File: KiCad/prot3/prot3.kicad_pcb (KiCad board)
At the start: 2 copper layers, 140 x 140 mm, 198 parts, among them J1 Conn_01x02_Socket, J2 LED_SW, J3 Conn_01x04_Socket, Q1 Q_Photo_NPN, Q10 Q_Photo_NPN, Q11 Q_Photo_NPN, Q12 Q_Photo_NPN, Q13 Q_Photo_NPN, Q14 Q_Photo_NPN, Q15 Q_Photo_NPN, Q16 Q_Photo_NPN, Q17 Q_Photo_NPN, Q18 Q_Photo_NPN, Q19 Q_Photo_NPN, Q2 Q_Photo_NPN, Q20 Q_Photo_NPN, Q21 Q_Photo_NPN, Q22 Q_Photo_NPN, Q23 Q_Photo_NPN, Q24 Q_Photo_NPN, Q25 Q_Photo_NPN, Q26 Q_Photo_NPN, Q27 Q_Photo_NPN, Q28 Q_Photo_NPN, Q29 Q_Photo_NPN, Q3 Q_Photo_NPN, Q30 Q_Photo_NPN, Q31 Q_Photo_NPN, Q32 Q_Photo_NPN, Q4 Q_Photo_NPN, Q5 Q_Photo_NPN, Q6 Q_Photo_NPN, Q7 Q_Photo_NPN, Q8 Q_Photo_NPN, Q9 Q_Photo_NPN, U1 LM339, U2 LM339, U3 LM339, U4 LM339, U5 LM339, U6 LM339, U7 LM339, U8 LM339

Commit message: コンパレーター割当て途中
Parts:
- moved C14 133.4 mm to (526.1, 463.9)
- moved C15 133.4 mm to (526.1, 466.5)
- moved R1 133.4 mm to (526.1, 469.0)
- moved B1 120.3 mm to (525.6, 473.4)
- moved C8 107.1 mm to (532.6, 550.0), turned to -157.5 degrees
- moved C11 104.3 mm to (544.6, 480.9), turned to 90 degrees
- moved U8 98.6 mm to (526.3, 552.0), turned to 22.5 degrees
- moved Rc29 98.6 mm to (519.6, 553.0), turned to 22.5 degrees
- moved Rc31 93.6 mm to (531.6, 547.3), turned to -157.5 degrees
- moved Rc30 93.3 mm to (518.5, 550.3), turned to 22.5 degrees
- moved RP2040_Zero1 92.7 mm to (542.0, 479.0), turned to 90 degrees
- moved Rc32 88.6 mm to (530.5, 544.6), turned to -157.5 degrees
- moved C7 80.2 mm to (479.0, 554.4), turned to 157.5 degrees
- moved C9 77.0 mm to (532.8, 492.9)
- moved Rc25 75.3 mm to (467.2, 548.0), turned to -22.5 degrees
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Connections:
- C1 pad 2: LED_5V -> GND
- C10 pad 2: LED_5V -> GND
- C11 pad 2: LED_5V -> GND
- C12 pad 2: LED_5V -> GND
- C13 pad 2: LED_5V -> GND
- C15 pad 2: LED_5V -> GND
- C2 pad 2: LED_5V -> GND
- C3 pad 2: LED_5V -> GND
- C4 pad 2: LED_5V -> GND
- C5 pad 2: LED_5V -> GND
- C6 pad 2: LED_5V -> GND
- C7 pad 2: LED_5V -> GND
- C8 pad 2: LED_5V -> GND
- C9 pad 2: LED_5V -> GND
- J1 pad 2: LED_5V -> GND
- J3 pad 4: LED_5V -> GND
- Q1 pad 2: Net-(Q1-E) -> 1D
- Q10 pad 2: Net-(Q10-E) -> 3C
- Q11 pad 2: Net-(Q11-E) -> 4A
- Q12 pad 2: Net-(Q12-E) -> 4B
- Q13 pad 2: Net-(Q13-E) -> 4D
- Q14 pad 2: Net-(Q14-E) -> 4C
- Q15 pad 2: Net-(Q15-E) -> 5A
- Q16 pad 2: Net-(Q16-E) -> 5B
- Q17 pad 2: Net-(Q17-E) -> 5D
- Q18 pad 2: Net-(Q18-E) -> 6A
- Q19 pad 2: Net-(Q19-E) -> 6B
- Q2 pad 2: Net-(Q2-E) -> 1C
- Q20 pad 2: Net-(Q20-E) -> 6D
- Q21 pad 2: Net-(Q21-E) -> 7A
- Q22 pad 2: Net-(Q22-E) -> 7B
- Q23 pad 2: Net-(Q23-E) -> 7D
- Q24 pad 2: Net-(Q24-E) -> 7C
- Q25 pad 2: Net-(Q25-E) -> 8A
- Q26 pad 2: Net-(Q26-E) -> 8B
- Q27 pad 2: Net-(Q27-E) -> 8B
- Q28 pad 2: Net-(Q28-E) -> 8A
- Q29 pad 2: Net-(Q29-E) -> 8D
- Q3 pad 2: Net-(Q3-E) -> 2B
- Q30 pad 2: Net-(Q30-E) -> 8C
- Q31 pad 2: Net-(Q31-E) -> 1A
- Q32 pad 2: Net-(Q32-E) -> 1B
- Q4 pad 2: Net-(Q4-E) -> 2A
- Q5 pad 2: Net-(Q5-E) -> 2D
- Q6 pad 2: Net-(Q6-E) -> 2C
- Q7 pad 2: Net-(Q7-E) -> 3A
- Q8 pad 2: Net-(Q8-E) -> 3B
- Q9 pad 2: Net-(Q9-E) -> 3D
- RP2040_Zero1 pad 22: LED_5V -> GND
- RP2040_Zero2 pad 22: LED_5V -> GND
- RV1 pad 3: LED_5V -> GND
- Rl1 pad 2: LED_5V -> GND
- Rl10 pad 2: LED_5V -> GND
- Rl11 pad 2: LED_5V -> GND
- Rl12 pad 2: LED_5V -> GND
- Rl13 pad 2: LED_5V -> GND
- Rl14 pad 2: LED_5V -> GND
- Rl15 pad 2: LED_5V -> GND
- Rl16 pad 2: LED_5V -> GND
- Rl17 pad 2: LED_5V -> GND
- Rl18 pad 2: LED_5V -> GND
- Rl19 pad 2: LED_5V -> GND
- Rl2 pad 2: LED_5V -> GND
- Rl20 pad 2: LED_5V -> GND
- Rl21 pad 2: LED_5V -> GND
- Rl22 pad 2: LED_5V -> GND
- Rl23 pad 2: LED_5V -> GND
- Rl24 pad 2: LED_5V -> GND
- Rl25 pad 2: LED_5V -> GND
- Rl26 pad 2: LED_5V -> GND
- Rl27 pad 2: LED_5V -> GND
- Rl28 pad 2: LED_5V -> GND
- Rl29 pad 2: LED_5V -> GND
- Rl3 pad 2: LED_5V -> GND
- Rl30 pad 2: LED_5V -> GND
- Rl31 pad 2: LED_5V -> GND
- Rl32 pad 2: LED_5V -> GND
- Rl4 pad 2: LED_5V -> GND
- Rl5 pad 2: LED_5V -> GND
- Rl6 pad 2: LED_5V -> GND
- Rl7 pad 2: LED_5V -> GND
- Rl8 pad 2: LED_5V -> GND
- Rl9 pad 2: LED_5V -> GND
- Rs1 pad 1: Net-(Q1-E) -> 1D
- Rs1 pad 2: LED_5V -> GND
- Rs10 pad 1: Net-(Q10-E) -> 3C
- Rs10 pad 2: LED_5V -> GND
- Rs11 pad 1: Net-(Q11-E) -> 4A
- Rs11 pad 2: LED_5V -> GND
- Rs12 pad 1: Net-(Q12-E) -> 4B
- Rs12 pad 2: LED_5V -> GND
- Rs13 pad 1: Net-(Q13-E) -> 4D
- Rs13 pad 2: LED_5V -> GND
- Rs14 pad 1: Net-(Q14-E) -> 4C
- Rs14 pad 2: LED_5V -> GND
- Rs15 pad 1: Net-(Q15-E) -> 5A
- Rs15 pad 2: LED_5V -> GND
- Rs16 pad 1: Net-(Q16-E) -> 5B
- Rs16 pad 2: LED_5V -> GND
- Rs17 pad 1: Net-(Q17-E) -> 5D
- Rs17 pad 2: LED_5V -> GND
- Rs18 pad 1: Net-(Q18-E) -> 6A
- Rs18 pad 2: LED_5V -> GND
- Rs19 pad 1: Net-(Q19-E) -> 6B
- Rs19 pad 2: LED_5V -> GND
- Rs2 pad 1: Net-(Q2-E) -> 1C
- Rs2 pad 2: LED_5V -> GND
- Rs20 pad 1: Net-(Q20-E) -> 6D
- Rs20 pad 2: LED_5V -> GND
- Rs21 pad 1: Net-(Q21-E) -> 7A
- Rs21 pad 2: LED_5V -> GND
- Rs22 pad 1: Net-(Q22-E) -> 7B
- Rs22 pad 2: LED_5V -> GND
- Rs23 pad 1: Net-(Q23-E) -> 7D
- Rs23 pad 2: LED_5V -> GND
- Rs24 pad 1: Net-(Q24-E) -> 7C
- Rs24 pad 2: LED_5V -> GND
- Rs25 pad 1: Net-(Q25-E) -> 8A
- Rs25 pad 2: LED_5V -> GND
- Rs26 pad 1: Net-(Q26-E) -> 8B
- Rs26 pad 2: LED_5V -> GND
- Rs27 pad 1: Net-(Q27-E) -> 8B
- Rs27 pad 2: LED_5V -> GND
- Rs28 pad 1: Net-(Q28-E) -> 8A
- Rs28 pad 2: LED_5V -> GND
- Rs29 pad 1: Net-(Q29-E) -> 8D
- Rs29 pad 2: LED_5V -> GND
- Rs3 pad 1: Net-(Q3-E) -> 2B
- Rs3 pad 2: LED_5V -> GND
- Rs30 pad 1: Net-(Q30-E) -> 8C
- Rs30 pad 2: LED_5V -> GND
- Rs31 pad 1: Net-(Q31-E) -> 1A
- Rs31 pad 2: LED_5V -> GND
- Rs32 pad 1: Net-(Q32-E) -> 1B
- Rs32 pad 2: LED_5V -> GND
- Rs4 pad 1: Net-(Q4-E) -> 2A
- Rs4 pad 2: LED_5V -> GND
- Rs5 pad 1: Net-(Q5-E) -> 2D
- Rs5 pad 2: LED_5V -> GND
- Rs6 pad 1: Net-(Q6-E) -> 2C
- Rs6 pad 2: LED_5V -> GND
- Rs7 pad 1: Net-(Q7-E) -> 3A
- Rs7 pad 2: LED_5V -> GND
- Rs8 pad 1: Net-(Q8-E) -> 3B
- Rs8 pad 2: LED_5V -> GND
- Rs9 pad 1: Net-(Q9-E) -> 3D
- Rs9 pad 2: LED_5V -> GND
- U1 pad 12: LED_5V -> GND
- U2 pad 12: LED_5V -> GND
- U3 pad 12: LED_5V -> GND
- U4 pad 12: LED_5V -> GND
- U5 pad 12: LED_5V -> GND
- U6 pad 12: LED_5V -> GND
- U7 pad 12: LED_5V -> GND
- U8 pad 12: LED_5V -> GND
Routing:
- net VCC: track 38.6 -> 146.4 mm
- net 8C: track 0.00 -> 38.2 mm
- net 6A: track 0.00 -> 35.5 mm
- net 8A: track 0.00 -> 32.1 mm
- net 5A: track 0.00 -> 29.5 mm
- net 3A: track 0.00 -> 27.9 mm
- net 4A: track 0.00 -> 27.7 mm
- net 1A: track 0.00 -> 26.2 mm
- net 8D: track 0.00 -> 25.3 mm
- net GND: track 0.00 -> 23.7 mm, vias 0 -> 2
- net 7C: track 0.00 -> 22.6 mm
- net 2C: track 0.00 -> 21.8 mm
- net 2B: track 0.00 -> 21.5 mm
- net 1C: track 0.00 -> 20.8 mm
- net 6B: track 0.00 -> 20.3 mm
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
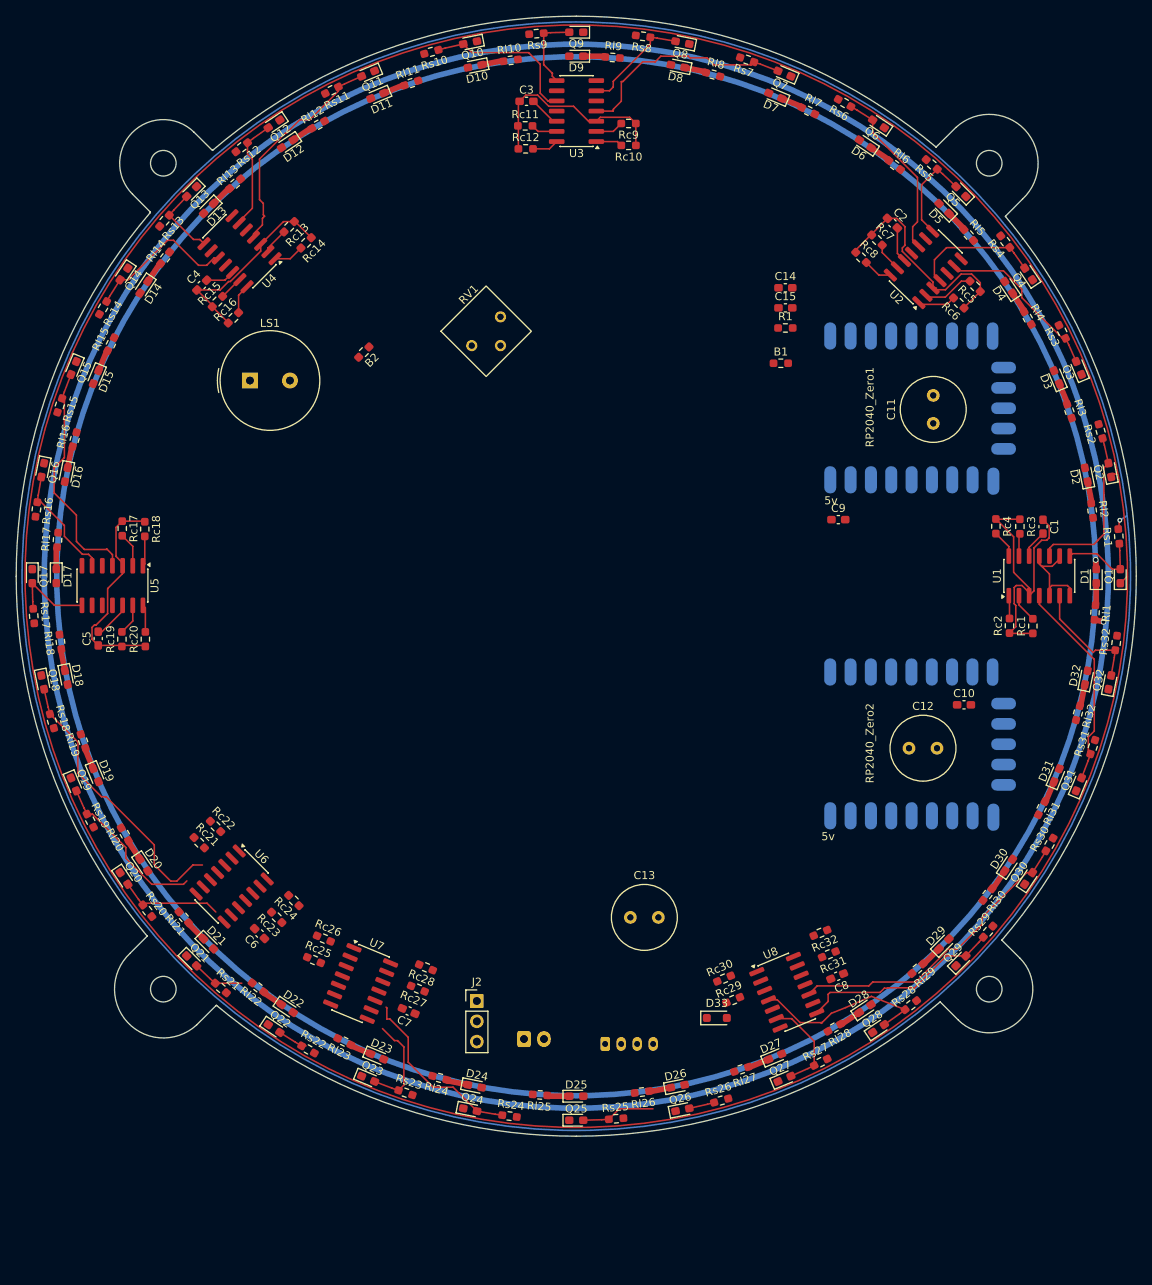
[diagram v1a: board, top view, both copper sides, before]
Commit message: conp+一周、センサーch割当てまで
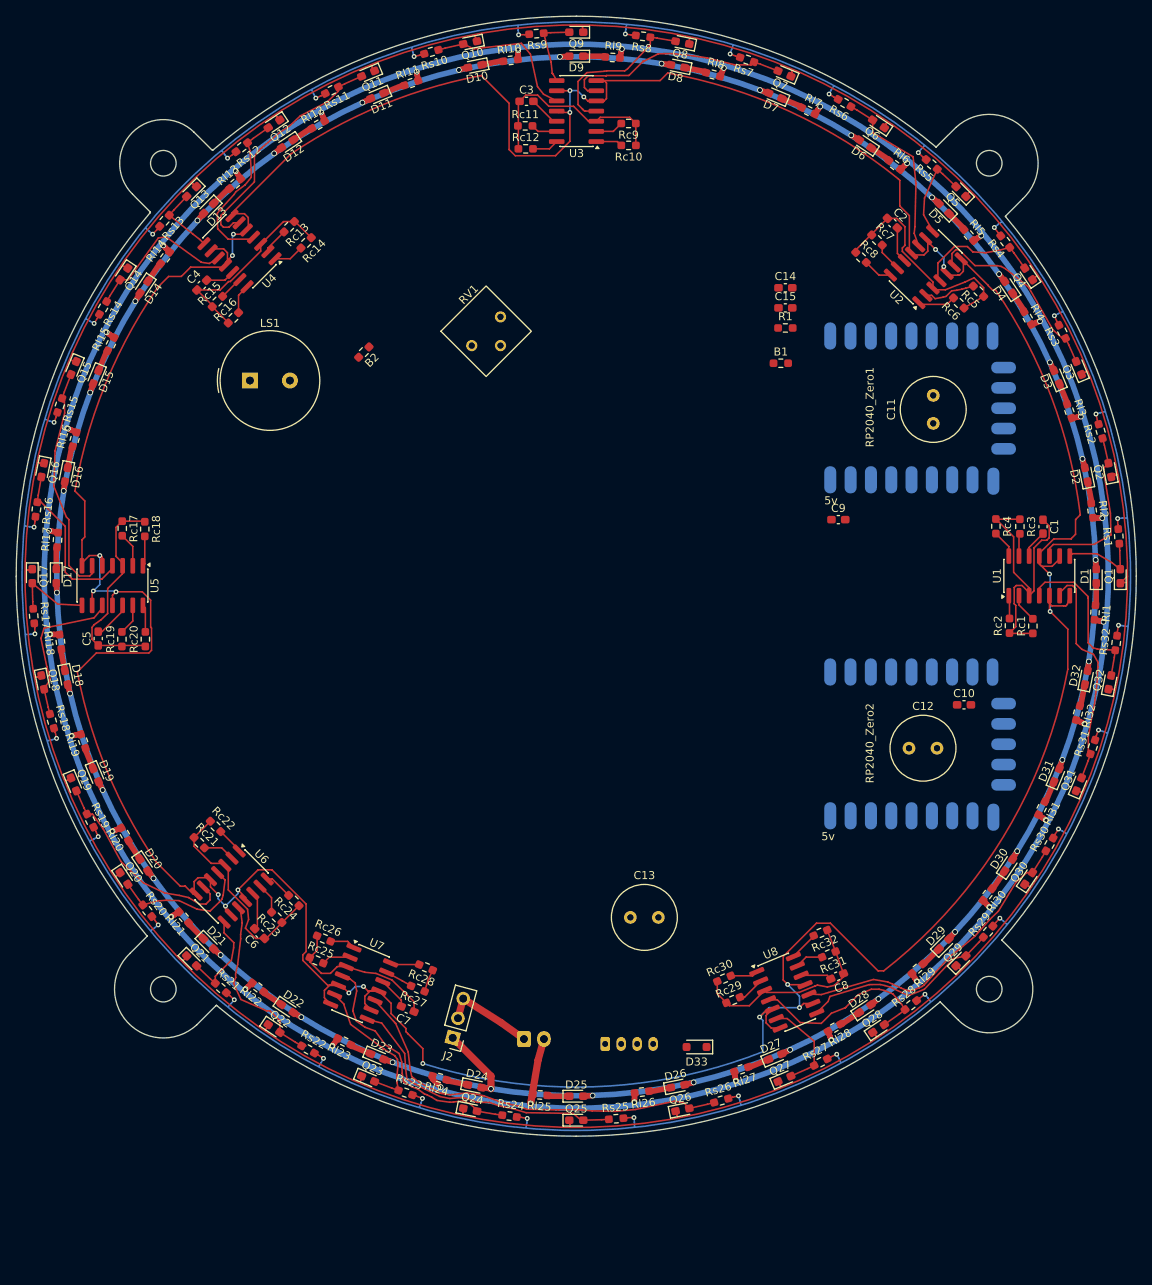
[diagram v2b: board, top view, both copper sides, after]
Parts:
- moved J2 5.51 mm to (484.6, 557.7), turned to 165 degrees
- moved D33 4.42 mm to (515.0, 558.9), turned to 180 degrees
- moved Rc5 0.75 mm to (550.3, 464.4)
- moved Rc25 0.32 mm to (467.5, 548.0)
- moved C7 0.28 mm to (478.9, 554.1)
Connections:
- J1 pad 1: LED_5V -> Net-(J1-Pin_1)
- J2 pad 1: Net-(J2-Pin_1) -> LED_5V
- J2 pad 2: Net-(J2-Pin_1) -> Net-(J1-Pin_1)
- J2 pad 3: LED_5V -> Net-(J1-Pin_1)
- Q11 pad 2: 4A -> 4B
- Q12 pad 2: 4B -> 4A
- Q15 pad 2: 5A -> 5B
- Q16 pad 2: 5B -> 5A
- Q18 pad 2: 6A -> 5C
- Q20 pad 2: 6D -> 6A
- Q21 pad 2: 7A -> 6D
- Q22 pad 2: 7B -> 6C
- Q23 pad 2: 7D -> 7B
- Q24 pad 2: 7C -> 7A
- Q25 pad 2: 8A -> 7D
- Q26 pad 2: 8B -> 7C
- Q31 pad 2: 1A -> 1B
- Q32 pad 2: 1B -> 1A
- Q7 pad 2: 3A -> 3B
- Q8 pad 2: 3B -> 3A
- Rs11 pad 1: 4A -> 4B
- Rs12 pad 1: 4B -> 4A
- Rs15 pad 1: 5A -> 5B
- Rs16 pad 1: 5B -> 5A
- Rs18 pad 1: 6A -> 5C
- Rs20 pad 1: 6D -> 6A
- Rs21 pad 1: 7A -> 6D
- Rs22 pad 1: 7B -> 6C
- Rs23 pad 1: 7D -> 7B
- Rs24 pad 1: 7C -> 7A
- Rs25 pad 1: 8A -> 7D
- Rs26 pad 1: 8B -> 7C
- Rs31 pad 1: 1A -> 1B
- Rs32 pad 1: 1B -> 1A
- Rs7 pad 1: 3A -> 3B
- Rs8 pad 1: 3B -> 3A
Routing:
- net conp_+: track 13.6 -> 307.3 mm, vias 0 -> 21
- net GND: track 23.7 -> 157.0 mm, vias 2 -> 64
- net VCC: track 146.4 -> 247.8 mm
- net LED_5V: track 1.17 -> 45.7 mm, vias 1 -> 32
- net 7C: track 22.6 -> 50.2 mm
- net 7A: track 6.51 -> 30.8 mm
- net 7D: track 12.5 -> 36.3 mm
- net 6C: track 0.00 -> 22.8 mm
- net 5C: track 0.00 -> 19.6 mm
- net 6A: track 35.5 -> 18.1 mm
- net 4B: track 14.1 -> 30.3 mm
- net 3B: track 13.6 -> 28.7 mm
- net 7B: track 3.75 -> 18.8 mm
- net 5B: track 14.7 -> 29.3 mm
- net 1B: track 14.9 -> 28.5 mm
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
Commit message: IMU用コンデンサ変更
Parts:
- added C16: C, Capacitor_SMD:C_0603_1608Metric_Pad1.08x0.95mm_HandSolder, B.Cu at (534.3, 535.1)
- added C17: C, Capacitor_SMD:C_0603_1608Metric_Pad1.08x0.95mm_HandSolder, B.Cu at (531.6, 535.1)
- added C18: C, Capacitor_SMD:C_0603_1608Metric_Pad1.08x0.95mm_HandSolder, B.Cu at (496.9, 555.3)
- C10, C9: moved to B.Cu
- C11, C12, C13: value C_Polarized_Small_US -> C; footprint Capacitor_THT:C_Radial_D8.0mm_H11.5mm_P3.50mm -> Capacitor_SMD:C_0603_1608Metric_Pad1.08x0.95mm_HandSolder; moved to B.Cu
- moved C12 30.1 mm to (534.8, 492.2), turned to 90 degrees
- moved C10 22.1 mm to (537.2, 535.1), turned to -90 degrees
- moved C13 14.1 mm to (496.9, 552.8), turned to 180 degrees
- moved C11 13.3 mm to (537.6, 492.2)
- moved C9 7.83 mm to (540.6, 492.3), turned to 90 degrees
- moved Rc29 3.16 mm to (520.2, 556.1)
- moved Rc30 3.16 mm to (519.1, 553.4)
- moved D33 2.63 mm to (514.0, 556.5), turned to -90 degrees
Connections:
- RP2040_Zero1 pad 1: OUT_TX -> unconnected-(RP2040_Zero1-0-Pad1)
- RP2040_Zero1 pad 2: OUT_RX -> unconnected-(RP2040_Zero1-1-Pad2)
- RP2040_Zero2 pad 1: unconnected-(RP2040_Zero2-0-Pad1) -> OUT_TX
- RP2040_Zero2 pad 2: unconnected-(RP2040_Zero2-1-Pad2) -> OUT_RX
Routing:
- net GND: track 157.0 -> 272.3 mm, vias 64 -> 66
- net IMU_5V: track 0.00 -> 112.6 mm, vias 0 -> 2
- net 1: track 3.60 -> 17.6 mm, vias 0 -> 1
- net 29: track 3.43 -> 17.0 mm, vias 0 -> 1
- net 30: track 3.46 -> 16.1 mm, vias 0 -> 1
- net 2: track 2.88 -> 14.9 mm, vias 0 -> 1
- net Net-(D33-A): track 0.00 -> 7.21 mm
- net 4: track 3.48 -> 8.95 mm, vias 0 -> 1
- net 32: track 3.66 -> 8.35 mm, vias 0 -> 1
- net 31: track 3.56 -> 7.60 mm, vias 0 -> 1
- net 3: track 2.83 -> 6.41 mm, vias 0 -> 1
- net VCC: track 247.8 -> 250.1 mm
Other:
- board text added: "5v"

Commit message: コンパレーターデジタル信号配線開始
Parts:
- moved RV1 15.4 mm to (475.5, 477.3), turned to 0 degrees
- moved B2 11.5 mm to (472.0, 483.4), turned to 0 degrees
- moved R1 2.21 mm to (528.2, 469.8)
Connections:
- RP2040_Zero1 pad 13: unconnected-(RP2040_Zero1-12-Pad13) -> RP1_TX
- RP2040_Zero1 pad 14: unconnected-(RP2040_Zero1-13-Pad14) -> RP1_RX
- RP2040_Zero2 pad 5: unconnected-(RP2040_Zero2-4-Pad5) -> RP1_RX
- RP2040_Zero2 pad 6: unconnected-(RP2040_Zero2-5-Pad6) -> RP1_TX
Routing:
- net VCC: track 250.1 -> 312.7 mm, vias 0 -> 3
- net RP1_RX: track 0.00 -> 44.2 mm
- net RP1_TX: track 0.00 -> 40.6 mm
- net (no net): track 0.00 -> 33.9 mm, vias 0 -> 2
- net unconnected-(RP2040_Zero1-11-Pad12): track 0.00 -> 30.0 mm, vias 0 -> 1
- net 8: track 3.67 -> 26.1 mm
- net unconnected-(RP2040_Zero1-28-Pad19): track 0.00 -> 21.3 mm, vias 0 -> 1
- net unconnected-(RP2040_Zero1-15-Pad16): track 0.00 -> 21.1 mm, vias 0 -> 1
- net unconnected-(RP2040_Zero1-8-Pad9): track 0.00 -> 20.6 mm, vias 0 -> 1
- net unconnected-(RP2040_Zero1-29-Pad20): track 0.00 -> 19.4 mm, vias 0 -> 1
- net Net-(RP2040_Zero1-7): track 0.00 -> 19.2 mm, vias 0 -> 1
- net 7: track 3.62 -> 22.0 mm
- net unconnected-(RP2040_Zero1-6-Pad7): track 0.00 -> 18.2 mm, vias 0 -> 1
- net GND: track 272.3 -> 286.3 mm, vias 66 -> 68
- net unconnected-(RP2040_Zero1-14-Pad15): track 0.00 -> 10.8 mm, vias 0 -> 1
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
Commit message: バイブコーディングはうんこ
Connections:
- RP2040_Zero1 pad 10: unconnected-(RP2040_Zero1-9-Pad10) -> 7
- RP2040_Zero1 pad 11: unconnected-(RP2040_Zero1-10-Pad11) -> 8
- RP2040_Zero1 pad 15: unconnected-(RP2040_Zero1-14-Pad15) -> 6
- RP2040_Zero1 pad 16: unconnected-(RP2040_Zero1-15-Pad16) -> 5
- RP2040_Zero1 pad 17: unconnected-(RP2040_Zero1-26-Pad17) -> 3
- RP2040_Zero1 pad 18: unconnected-(RP2040_Zero1-27-Pad18) -> 4
- RP2040_Zero1 pad 19: unconnected-(RP2040_Zero1-28-Pad19) -> 2
- RP2040_Zero1 pad 20: unconnected-(RP2040_Zero1-29-Pad20) -> 1
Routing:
- net (no net): track 33.9 -> 0.00 mm, vias 2 -> 0
- net 5: track 15.8 -> 38.6 mm, vias 0 -> 1
- net 2: track 4.90 -> 27.4 mm, vias 0 -> 1
- net unconnected-(RP2040_Zero1-28-Pad19): track 21.3 -> 0.00 mm, vias 1 -> 0
- net unconnected-(RP2040_Zero1-15-Pad16): track 21.1 -> 0.00 mm, vias 1 -> 0
- net 1: track 19.6 -> 40.5 mm, vias 0 -> 1
- net unconnected-(RP2040_Zero1-29-Pad20): track 19.4 -> 0.00 mm, vias 1 -> 0
- net 6: track 13.4 -> 30.9 mm, vias 0 -> 1
- net 7: track 22.0 -> 34.6 mm, vias 0 -> 1
- net unconnected-(RP2040_Zero1-14-Pad15): track 10.8 -> 0.00 mm, vias 1 -> 0
- net 4: track 8.40 -> 14.9 mm, vias 0 -> 1
- net 8: track 26.1 -> 31.8 mm, vias 0 -> 1
- net unconnected-(RP2040_Zero1-27-Pad18): track 4.45 -> 0.00 mm, vias 1 -> 0
- net 3: track 11.8 -> 15.6 mm, vias 2 -> 3
- net unconnected-(RP2040_Zero1-26-Pad17): track 2.59 -> 0.00 mm, vias 1 -> 0
